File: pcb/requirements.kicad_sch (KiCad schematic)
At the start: 0 parts

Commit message: Change schematic name
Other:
- title: Environment Module -> Client
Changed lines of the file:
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@@
 	(paper "A4")
 	(title_block
-		(title "Environment Module")
+		(title "Client")
 		(date "<<release-date>>")
 		(rev "<<tag>>")
@@
 		)
 	)
-	(text_box "BASIC\n\n* Wireless to send/rcv commands\n* 4 PWM/Servo Outputs\n* 2 Relay Outputs\n* 1 ADC\n* 1 I2C Bus\n* 2 Power Ports - In & Out"
+	(text_box "BASIC\n\n* Wireless to send/rcv commands\n* 4 PWM/Servo Outputs\n* 2 Relay Outputs\n* 2 ADC\n* I2C Bus\n* Power Ports - 5V & 3.3V In\n* USB Data + Power"
 		(exclude_from_sim yes)
 		(at 17.78 30.48 0)
@@
 		)
 	)
-	(text_box "Interfaces:\n* 2 - Power\n* 1 - Serial\n* 1 - Programming/Debug\n\nOUTPUT:\n* On Board Status LEDs\n* External LED Port\n* 1 5V Power\n* 1 3.3V Power"
+	(text_box "Interfaces:\n* 2 - Power\n* 1 - Serial\n* 1 - Programming/Debug\n* 2 - I2C\n\nOUTPUT:\n* On Board Status LEDs\n* External LED Port\n* 1 5V Power\n* 1 3.3V Power"
 		(exclude_from_sim yes)
 		(at 189.992 30.48 0)
@@
 		)
 	)
-	(text_box "Environment Sensors\n\n* Temperature\n* Light\n* Humidity\n* VOC\n* CO2\n* NOX"
+	(text_box "Environment Sensors\n\n* Temperature\n* Light\n* Humidity\n* VOC\n* Particle\n* CO2\n* NOX"
 		(exclude_from_sim yes)
 		(at 103.886 30.48 0)

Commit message: Updated project name and properties
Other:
- title: Client -> Client Hardware
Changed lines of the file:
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@@
 	(paper "A4")
 	(title_block
-		(title "Client")
+		(title "Client Hardware")
 		(date "<<release-date>>")
 		(rev "<<tag>>")
@@
 		)
 	)
-	(text_box "Environment Sensors\n\n* Temperature\n* Light\n* Humidity\n* VOC\n* Particle\n* CO2\n* NOX"
+	(text_box "Sensors\n\n* Temperature\n* Light\n* Humidity\n* VOC\n* Particle\n* CO2\n* NOX"
 		(exclude_from_sim yes)
 		(at 103.886 30.48 0)

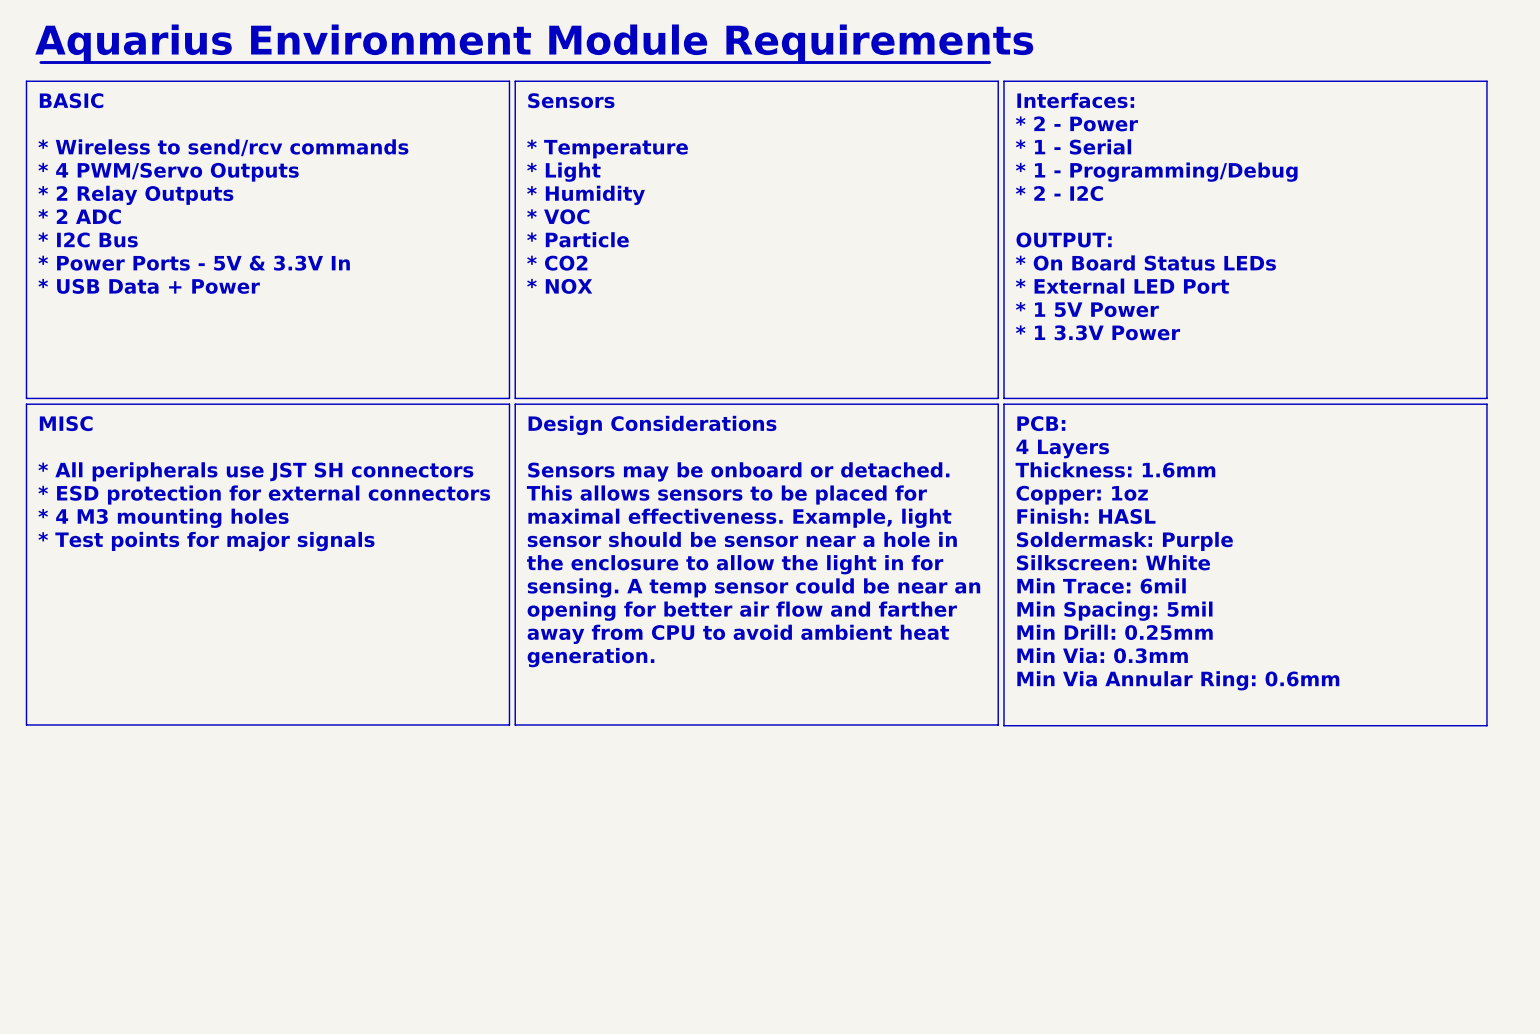
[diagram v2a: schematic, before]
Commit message: Added renders and aligned connectors
Added renders
Aligned connectors to grid
Added dimensions
Fixed part numbers and values
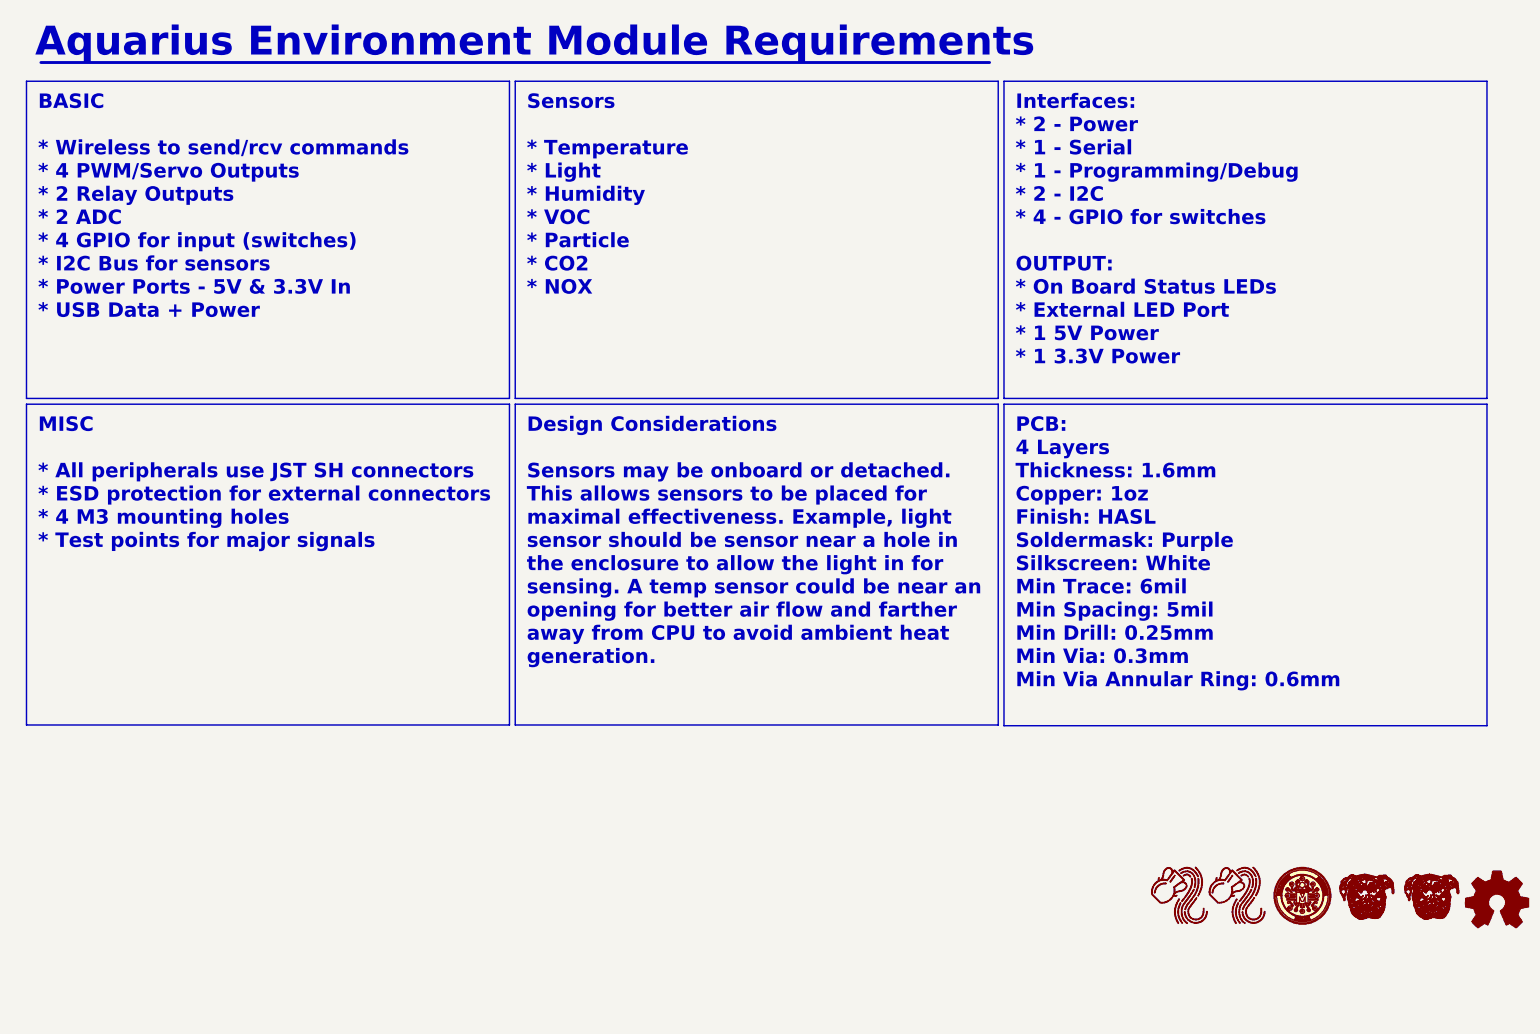
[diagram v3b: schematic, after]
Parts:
- added LOGO1: ~, CRGM Logos:CRGM Logo 10mm, symbol CRGM Logos:CRGM Logo
- added LOGO2, LOGO3: ~, CRGM Logos:Aquarius Logo 5mm, symbol CRGM Logos:Aquarius Logo
- added LOGO4: ~, Symbol:OSHW-Logo_5.7x6mm_SilkScreen, symbol Graphic:Logo_Open_Hardware_Small
- added LOGO5, LOGO6: ~, CRGM Logos:Roxy 6.5mm, symbol CRGM Logos:Roxy Logo
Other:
- title: Client Hardware -> Client

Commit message: Added RF connector; re-placed and re-routed
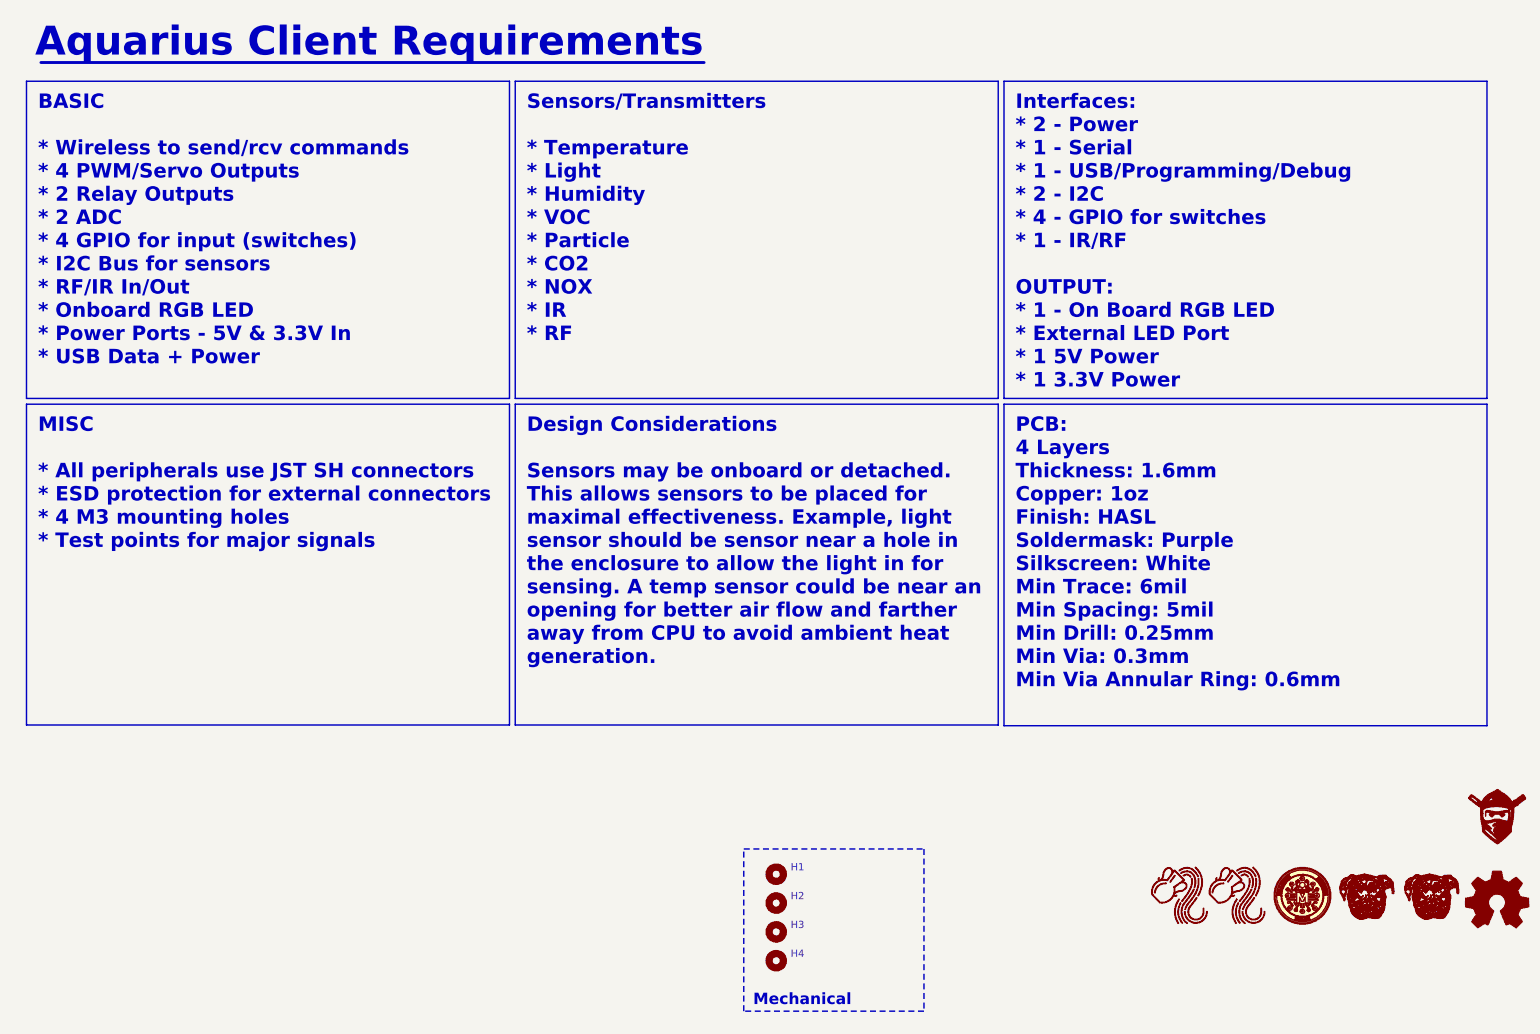
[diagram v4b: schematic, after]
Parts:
- added H1, H2, H3, H4: ~, CRGM Mechanical:MountingHole_3.2mm_M3_Pad_Via, symbol Mechanical:MountingHole
- added LOGO7: ~, CRGM Logos:FNWW Face 5mm, symbol CRGM Logos:FNWW Face
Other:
- note added: "Aquarius Client Requirements"
- note added: "Mechanical"
- note removed: "Aquarius Environment Module Requirements"
- title: Client -> Aquarius Client

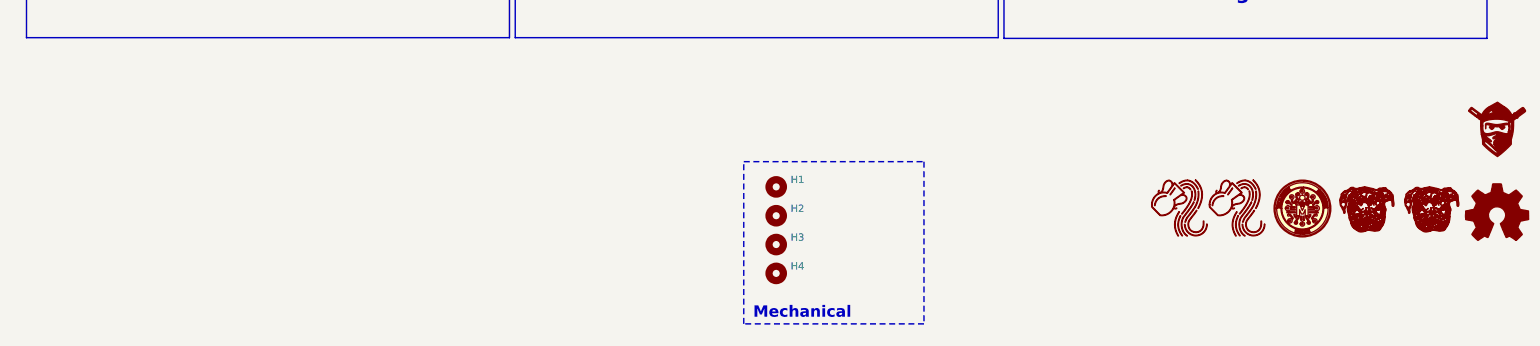
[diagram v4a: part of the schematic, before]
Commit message: Removed indictors sheet
Fixed attribute consistency with schematic and symbols
Moved logos to separate box
Updated DRC warnings/ignore
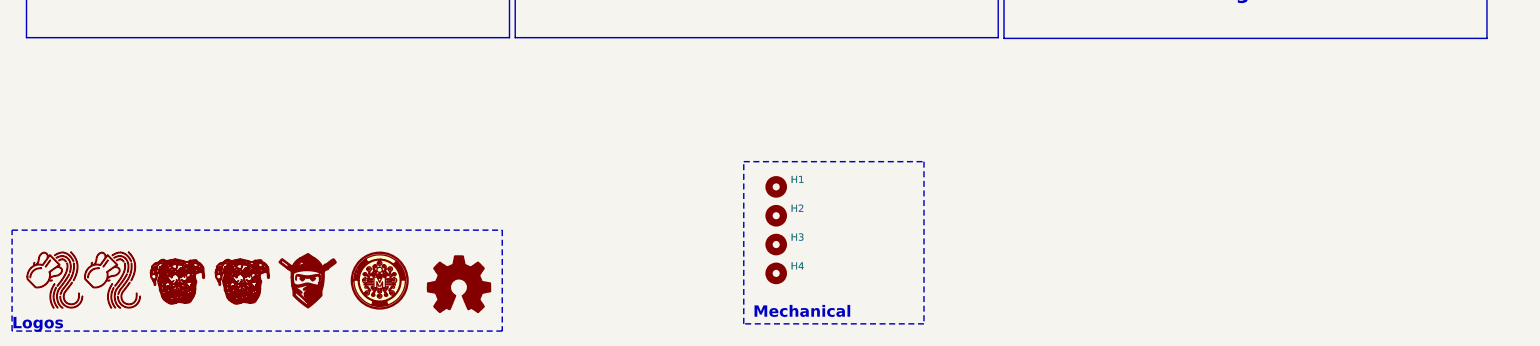
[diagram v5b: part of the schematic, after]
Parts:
- LOGO7: now left out of the parts list
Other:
- note added: "Logos"

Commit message: Added buzzer
Added buzzer
Fixed models
Updated images
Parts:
- LOGO3: footprint CRGM Logos:Aquarius Logo 5mm -> CRGM Logos:Aquarius Logo 8mm
- LOGO6: footprint CRGM Logos:Roxy 6.5mm -> CRGM Logos:Roxy 8mm
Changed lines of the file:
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@@
 			)
 		)
-		(property "Footprint" "CRGM Logos:Aquarius Logo 5mm"
+		(property "Footprint" "CRGM Logos:Aquarius Logo 8mm"
 			(at 24.384 189.738 0)
 			(effects
@@
 			)
 		)
-		(property "Footprint" "CRGM Logos:Roxy 6.5mm"
+		(property "Footprint" "CRGM Logos:Roxy 8mm"
 			(at 55.88 194.818 0)
 			(effects
